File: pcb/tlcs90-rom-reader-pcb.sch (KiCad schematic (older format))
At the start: 59 parts, among them J1 Conn_01x04, J2 Conn_Coaxial_Power, Q1 Q_NPN_ECB, SW1 SW_SPDT, SW2 SW_SPDT, SW3 SW_Push, SW4 SW_SPDT, U1 TMP90C840AN, U10 74LS08, U11 74LS04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

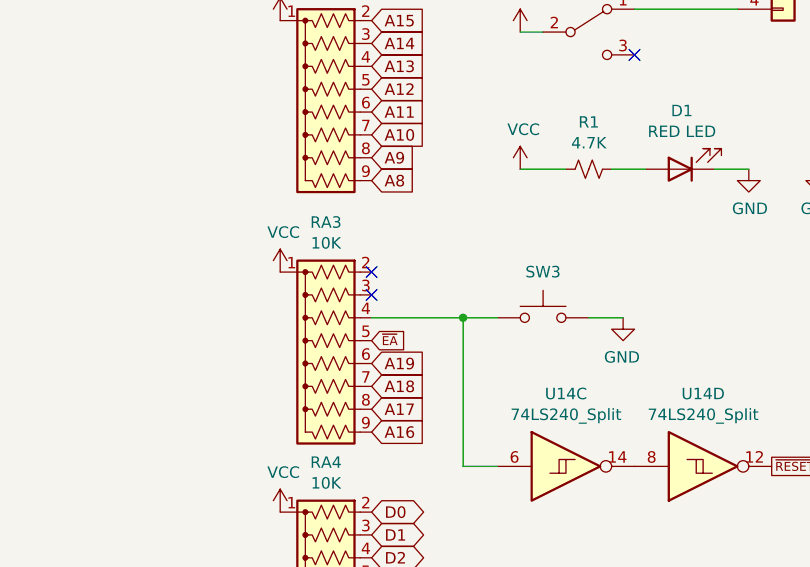
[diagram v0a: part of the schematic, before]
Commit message: new 3.1: added pull-up resistors to /RD and /WR signals
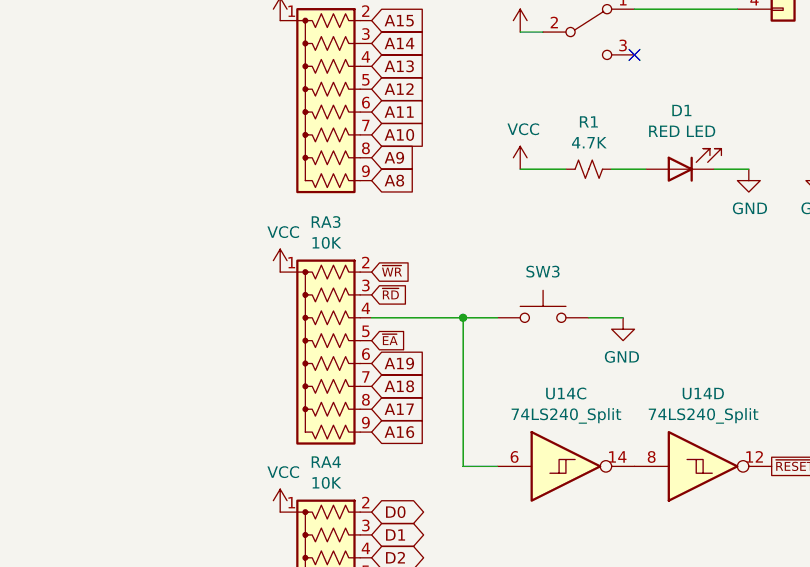
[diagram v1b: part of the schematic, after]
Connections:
- net ~RD: now also RA3.3 (R2)
- net ~WR: now also RA3.2 (R1)
- no-connect marks 40 -> 38
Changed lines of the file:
@@
 	-1   0    0    1
 $EndComp
-NoConn ~ 3900 3850
 Wire Wire Line
 	3150 7150 3200 7150
@@
 	10500 7600 10300 7600
 Connection ~ 10300 7600
-NoConn ~ 3900 3750
 Wire Wire Line
 	3200 8700 3200 9050
@@
 Text Notes 14800 5050 0    50   ~ 0
 EQUATIONS\n-------\n\no23 =\no22 = \no21 = \no20 = \no19 = \no18 = <new PC value>\no17 = <see PLD notes>\no16 = \n\n/o15 = i1\n\n/o14 = /i8 & i9 & i10 & i11 & i13
+Text GLabel 3900 3850 2    39   Input ~ 0
+~RD
+Text GLabel 3900 3750 2    39   Input ~ 0
+~WR
 $EndSCHEMATC

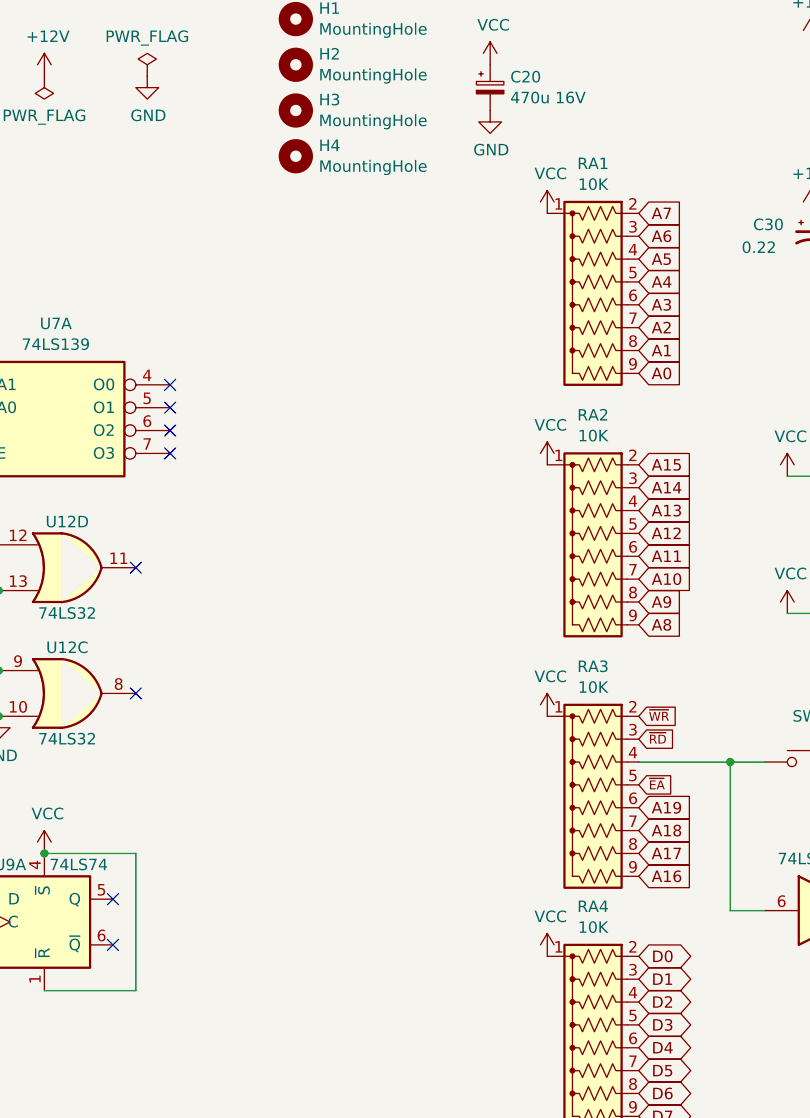
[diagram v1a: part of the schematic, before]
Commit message: update pcb: add selector to set Pull-up or Pull-down resistors on address and data buses
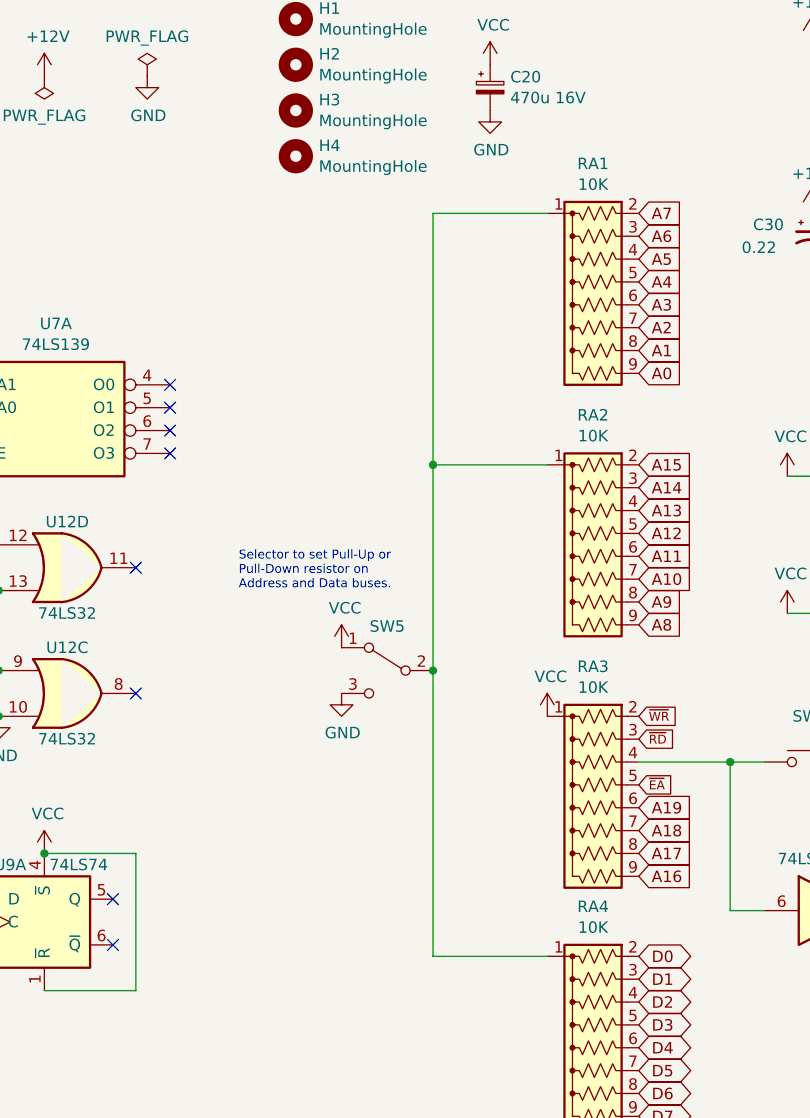
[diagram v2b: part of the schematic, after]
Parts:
- added SW5: PinHeader, Connector_PinHeader_2.54mm:PinHeader_1x03_P2.54mm_Vertical, symbol Switch:SW_SPDT
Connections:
- net GND: now also SW5.3 (C)
- net VCC: now also SW5.1 (A); no longer RA1.1 (common), RA2.1 (common), RA4.1 (common)
- new net: RA1.1 (common), RA2.1 (common), RA4.1 (common), SW5.2 (B)
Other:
- note added: "Selector to set Pull-Up or\nPull-Down resistor on\nAddress and Data buses."
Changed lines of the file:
@@
-	1    0    0    -1
-$EndComp
-$Comp
-L power:VCC #PWR0102
-U 1 1 656AE0B5
-P 3500 1550
-F 0 "#PWR0102" H 3500 1400 50  0001 C CNN
-F 1 "VCC" H 3515 1723 50  0000 C CNN
-F 2 "" H 3500 1550 50  0001 C CNN
-F 3 "" H 3500 1550 50  0001 C CNN
-	1    3500 1550
-	1    0    0    -1
-$EndComp
-$Comp
-L power:VCC #PWR0103
-U 1 1 656B7BD2
-P 3500 2650
-F 0 "#PWR0103" H 3500 2500 50  0001 C CNN
-F 1 "VCC" H 3515 2823 50  0000 C CNN
-F 2 "" H 3500 2650 50  0001 C CNN
-F 3 "" H 3500 2650 50  0001 C CNN
-	1    3500 2650
-	1    0    0    -1
-$EndComp
-$Comp
-L power:VCC #PWR0104
-U 1 1 656C1729
-P 3500 4800
-F 0 "#PWR0104" H 3500 4650 50  0001 C CNN
-F 1 "VCC" H 3515 4973 50  0000 C CNN
-F 2 "" H 3500 4800 50  0001 C CNN
-F 3 "" H 3500 4800 50  0001 C CNN
-	1    3500 4800
 	1    0    0    -1
 $EndComp
@@
 Text GLabel 3900 3750 2    39   Input ~ 0
 ~WR
+Wire Wire Line
+	3500 4800 3000 4800
+Wire Wire Line
+	3500 1550 3000 1550
+Text Notes 2150 3200 0    39   ~ 0
+Selector to set Pull-Up or\nPull-Down resistor on\nAddress and Data buses.
+Connection ~ 3000 3550
+Wire Wire Line
+	3000 4800 3000 3550
+$Comp
+L power:GND #PWR0102
+U 1 1 690F3EDC
+P 2600 3650
+F 0 "#PWR0102" H 2600 3400 50  0001 C CNN
+F 1 "GND" H 2605 3477 50  0000 C CNN
+F 2 "" H 2600 3650 50  0001 C CNN
+F 3 "" H 2600 3650 50  0001 C CNN
+	1    2600 3650
+	1    0    0    -1
+$EndComp
+$Comp
+L Switch:SW_SPDT SW5
+U 1 1 690D4E10
+P 2800 3550
+F 0 "SW5" H 2800 3743 50  0000 C CNN
+F 1 "PinHeader" H 2800 3744 50  0001 C CNN
+F 2 "Connector_PinHeader_2.54mm:PinHeader_1x03_P2.54mm_Vertical" H 2800 3550 50  0001 C CNN
+F 3 "~" H 2800 3550 50  0001 C CNN
+	1    2800 3550
+	-1   0    0    -1
+$EndComp
+$Comp
+L power:VCC #PWR0103
+U 1 1 656B7BD2
+P 2600 3450
+F 0 "#PWR0103" H 2600 3300 50  0001 C CNN
+F 1 "VCC" H 2615 3623 50  0000 C CNN
+F 2 "" H 2600 3450 50  0001 C CNN
+F 3 "" H 2600 3450 50  0001 C CNN
+	1    2600 3450
+	1    0    0    -1
+$EndComp
+Wire Wire Line
+	3000 1550 3000 2650
+Wire Wire Line
+	3500 2650 3000 2650
+Connection ~ 3000 2650
+Wire Wire Line
+	3000 2650 3000 3550
 $EndSCHEMATC
